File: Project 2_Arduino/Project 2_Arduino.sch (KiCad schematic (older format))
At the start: 16 parts, among them U2 LM1117-5.0, U3 ATMEGA328P-AU

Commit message: schematics USB UART added
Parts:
- added C4: 100nF, symbol C
- added U1: FT232RL, symbol FT232RL
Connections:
- wire segments 38 -> 48
- no-connect marks 0 -> 13
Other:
- moved on the sheet: C1, C3, C5, C7, R?, U3

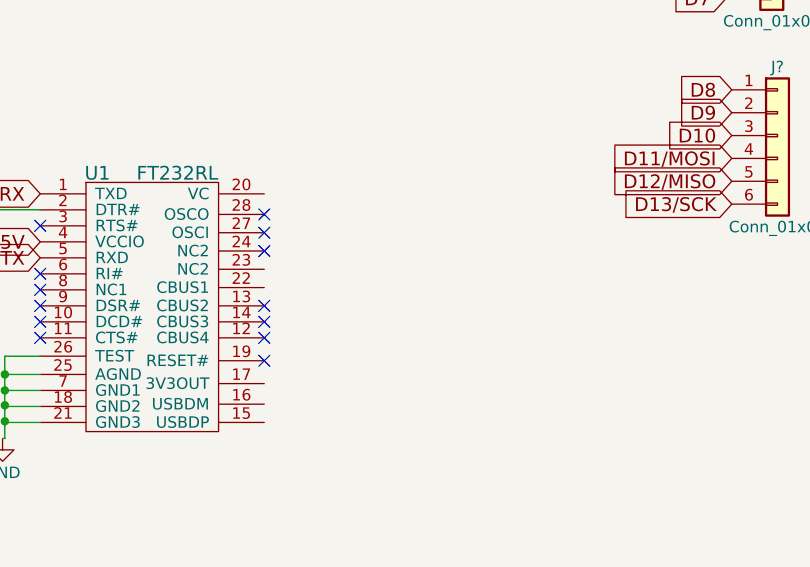
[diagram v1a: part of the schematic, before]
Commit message: USB to UART done
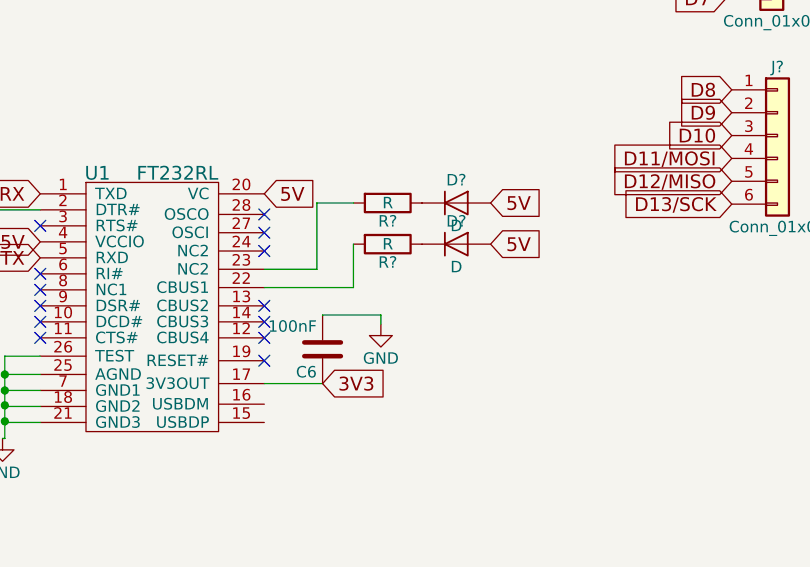
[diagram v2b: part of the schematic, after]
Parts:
- added C6: 100nF, symbol C
- added D? (x2): D, symbol D
- added R? (x2): R, symbol R
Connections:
- net labels added: 3V3
- wire segments 48 -> 56
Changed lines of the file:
@@
 Wire Wire Line
 	7095 4750 7085 4750
+Text GLabel 8230 3680 2    60   Input ~ 0
+5V
+$Comp
+L R R?
+U 1 1 59DF21B6
+P 8770 3900
+F 0 "R?" V 8850 3900 50  0000 C CNN
+F 1 "R" V 8770 3900 50  0000 C CNN
+F 2 "" V 8700 3900 50  0001 C CNN
+F 3 "" H 8770 3900 50  0001 C CNN
+	1    8770 3900
+	0    1    1    0
+$EndComp
+$Comp
+L D D?
+U 1 1 59DF2486
+P 9070 3720
+F 0 "D?" H 9070 3820 50  0000 C CNN
+F 1 "D" H 9070 3620 50  0000 C CNN
+F 2 "" H 9070 3720 50  0001 C CNN
+F 3 "" H 9070 3720 50  0001 C CNN
+	1    9070 3720
+	1    0    0    -1
+$EndComp
+$Comp
+L D D?
+U 1 1 59DF253A
+P 9070 3900
+F 0 "D?" H 9070 4000 50  0000 C CNN
+F 1 "D" H 9070 3800 50  0000 C CNN
+F 2 "" H 9070 3900 50  0001 C CNN
+F 3 "" H 9070 3900 50  0001 C CNN
+	1    9070 3900
+	1    0    0    -1
+$EndComp
+Text GLabel 9220 3720 2    60   Input ~ 0
+5V
+Text GLabel 9220 3900 2    60   Input ~ 0
+5V
+Wire Wire Line
+	8230 4090 8620 4090
+Wire Wire Line
+	8620 4090 8620 3900
+$Comp
+L R R?
+U 1 1 59DF2040
+P 8770 3720
+F 0 "R?" V 8850 3720 50  0000 C CNN
+F 1 "R" V 8770 3720 50  0000 C CNN
+F 2 "" V 8700 3720 50  0001 C CNN
+F 3 "" H 8770 3720 50  0001 C CNN
+	1    8770 3720
+	0    1    1    0
+$EndComp
+Wire Wire Line
+	8620 3720 8460 3720
+Wire Wire Line
+	8460 3720 8460 4010
+Wire Wire Line
+	8460 4010 8230 4010
+$Comp
+L C C6
+U 1 1 59DF2FE1
+P 8485 4360
+F 0 "C6" H 8510 4460 50  0000 L CNN
+F 1 "100nF" H 8510 4260 50  0000 L CNN
+F 2 "" H 8523 4210 50  0001 C CNN
+F 3 "" H 8485 4360 50  0001 C CNN
+	1    8485 4360
+	-1   0    0    1
+$EndComp
+Wire Wire Line
+	8230 4510 8485 4510
+Wire Wire Line
+	8485 4210 8740 4210
+Wire Wire Line
+	8740 4210 8740 4250
+$Comp
+L GND #PWR?
+U 1 1 59DF368B
+P 8740 4250
+F 0 "#PWR?" H 8740 4000 50  0001 C CNN
+F 1 "GND" H 8740 4100 50  0000 C CNN
+F 2 "" H 8740 4250 50  0001 C CNN
+F 3 "" H 8740 4250 50  0001 C CNN
+	1    8740 4250
+	1    0    0    -1
+$EndComp
+Text GLabel 8485 4510 2    60   Input ~ 0
+3V3
 $EndSCHEMATC

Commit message: first pass schematic done
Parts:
- removed C?: C, symbol C
- removed D?: D, symbol D
- removed R?: R, symbol R
- removed U2: LM1117-5.0, symbol LM1117-5.0
- added C2: 4.7uF_16V, symbol CP
- added C9: 100nF, symbol C
- added DL: D, symbol D
- added F1: Fuse, symbol Fuse
- added J3: USB_microB_2040002-1, symbol USB_microB_2040002-1
- added J4: Conn_02x03_Odd_Even, symbol Conn_02x03_Odd_Even
- added RD: 1K, symbol R
- added SW1: SW_Push, symbol SW_Push
- added Y1: 16MHz, symbol Crystal
- B, D, R2A, RA, RB: renamed from R?; value R -> 1K
- gave numbers to parts that had none: 3
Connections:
- net labels removed: VIN
- wire segments 56 -> 87
- no-connect marks 13 -> 14
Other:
- note added: "+5V Selector"
- note added: "Bypass Capacitors\n"
- note added: "Header Pins"
- note added: "ICSP\n"
- note added: "Microcontroller"
- note added: "Reset Switch"
- note added: "USB to UART"
- moved on the sheet: B, C1, C3, C4, C5, C6, C7, D, D1, DX1, DX2, J?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

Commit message: rearrange
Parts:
- gave numbers to parts that had none: 3
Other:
- moved on the sheet: B, C1, C2, C3, C4, C5, C6, C7, C9, D, D1, DL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

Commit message: caps edited
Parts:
- removed C2, C5: 4.7uF_16V, symbol CP
- added C2, C5: 10uF, symbol C
- added J13: Conn_01x03, symbol Conn_01x03
- renumbered DL to D3, RA to R1, RB to R2, B to R3, D to R4, R2A to R5, RD to R6
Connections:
- net D0 is gone; now on net D0/RX: J11.1 (Pin_1)
- net D1 is gone; now on net D1/TX: J11.2 (Pin_2)
- net 3V3: now also J13.2 (Pin_2)
- net 5V: now also C5.1, J13.1 (Pin_1)
- net GND: now also C2.2, C5.2, J13.3 (Pin_3)
- net VUSB: now also C2.1
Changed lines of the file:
@@
 $EndComp
 $Comp
-L GND #PWR?
+L GND #PWR01
 U 1 1 59DF0D4B
 P 1975 3875
-F 0 "#PWR?" H 1975 3625 50  0001 C CNN
+F 0 "#PWR01" H 1975 3625 50  0001 C CNN
 F 1 "GND" H 1975 3725 50  0000 C CNN
 F 2 "" H 1975 3875 50  0001 C CNN
@@
 A1
 Text GLabel 8700 5100 0    60   Input ~ 0
-D0
+D0/RX
 Text GLabel 8700 5200 0    60   Input ~ 0
-D1
+D1/TX
 Text GLabel 8700 5300 0    60   Input ~ 0
 D2
@@
 $EndComp
 $Comp
-L GND #PWR?
+L GND #PWR02
 U 1 1 59DEDBC3
 P 1825 2275
-F 0 "#PWR?" H 1825 2025 50  0001 C CNN
+F 0 "#PWR02" H 1825 2025 50  0001 C CNN
 F 1 "GND" H 1825 2125 50  0000 C CNN
 F 2 "" H 1825 2275 50  0001 C CNN
@@
 $EndComp
 $Comp
-L CP C5
-U 1 1 59DEDF72
-P 1100 1975
-F 0 "C5" H 1125 2075 50  0000 L CNN
-F 1 "4.7uF_16V" H 700 1875 50  0000 L CNN
-F 2 "" H 1138 1825 50  0001 C CNN
-F 3 "" H 1100 1975 50  0001 C CNN
-	1    1100 1975
-	1    0    0    -1
-$EndComp
-$Comp
-L GND #PWR?
+L GND #PWR03
 U 1 1 59DEE03F
 P 1375 2200
-F 0 "#PWR?" H 1375 1950 50  0001 C CNN
+F 0 "#PWR03" H 1375 1950 50  0001 C CNN
 F 1 "GND" H 1375 2050 50  0000 C CNN
 F 2 "" H 1375 2200 50  0001 C CNN
@@
 $EndComp
 $Comp
-L R R2A
+L R R5
 U 1 1 59DEEDB3
 P 4975 1600
-F 0 "R2A" V 5055 1600 50  0000 C CNN
+F 0 "R5" V 5055 1600 50  0000 C CNN
 F 1 "1K" V 4975 1600 50  0000 C CNN
 F 2 "" V 4905 1600 50  0001 C CNN
@@
 $EndComp
 $Comp
-L R RB
+L R R2
 U 1 1 59DEEEEE
 P 4950 3125
-F 0 "RB" V 5030 3125 50  0000 C CNN
+F 0 "R2" V 5030 3125 50  0000 C CNN
 F 1 "1K" V 4950 3125 50  0000 C CNN
 F 2 "" V 4880 3125 50  0001 C CNN
@@
 $EndComp
 $Comp
-L R RA
+L R R1
 U 1 1 59DEEF4E
 P 4950 3350
-F 0 "RA" V 5030 3350 50  0000 C CNN
+F 0 "R1" V 5030 3350 50  0000 C CNN
 F 1 "1K" V 4950 3350 50  0000 C CNN
 F 2 "" V 4880 3350 50  0001 C CNN
@@
 TX
 $Comp
-L GND #PWR?
+L GND #PWR04
 U 1 1 59DF0EF9
 P 7335 2650
-F 0 "#PWR?" H 7335 2400 50  0001 C CNN
+F 0 "#PWR04" H 7335 2400 50  0001 C CNN
 F 1 "GND" H 7335 2500 50  0000 C CNN
 F 2 "" H 7335 2650 50  0001 C CNN
@@
 5V
 $Comp
-L R D
+L R R4
 U 1 1 59DF21B6
 P 9020 1800
-F 0 "D" V 9100 1800 50  0000 C CNN
+F 0 "R4" V 9100 1800 50  0000 C CNN
 F 1 "1K" V 9020 1800 50  0000 C CNN
 F 2 "" V 8950 1800 50  0001 C CNN
@@
 5V
 $Comp
-L R B
+L R R3
 U 1 1 59DF2040
 P 9020 1620
-F 0 "B" V 9100 1620 50  0000 C CNN
+F 0 "R3" V 9100 1620 50  0000 C CNN
 F 1 "1K" V 9020 1620 50  0000 C CNN
 F 2 "" V 8950 1620 50  0001 C CNN
@@
 $EndComp
 $Comp
-L GND #PWR?
+L GND #PWR05
 U 1 1 59DF368B
 P 8990 2150
-F 0 "#PWR?" H 8990 1900 50  0001 C CNN
+F 0 "#PWR05" H 8990 1900 50  0001 C CNN
 F 1 "GND" H 8990 2000 50  0000 C CNN
 F 2 "" H 8990 2150 50  0001 C CNN
@@
 $EndComp
 $Comp
-L GND #PWR?
+L GND #PWR06
 U 1 1 59DF49F3
 P 10500 2475
-F 0 "#PWR?" H 10500 2225 50  0001 C CNN
+F 0 "#PWR06" H 10500 2225 50  0001 C CNN
 F 1 "GND" H 10500 2325 50  0000 C CNN
 F 2 "" H 10500 2475 50  0001 C CNN
@@
 D11/MOSI
 $Comp
-L GND #PWR?
+L GND #PWR07
 U 1 1 59DF7438
 P 5700 7125
-F 0 "#PWR?" H 5700 6875 50  0001 C CNN
+F 0 "#PWR07" H 5700 6875 50  0001 C CNN
 F 1 "GND" H 5700 6975 50  0000 C CNN
 F 2 "" H 5700 7125 50  0001 C CNN
@@
 $EndComp
 $Comp
-L GND #PWR?
+L GND #PWR08
 U 1 1 59DFC4DA
 P 1150 5925
-F 0 "#PWR?" H 1150 5675 50  0001 C CNN
+F 0 "#PWR08" H 1150 5675 50  0001 C CNN
 F 1 "GND" H 1150 5775 50  0000 C CNN
 F 2 "" H 1150 5925 50  0001 C CNN
@@
 RESET
 $Comp
-L R RD
+L R R6
 U 1 1 59DFCA3A
 P 1700 5675
-F 0 "RD" V 1780 5675 50  0000 C CNN
+F 0 "R6" V 1780 5675 50  0000 C CNN
 F 1 "1K" V 1700 5675 50  0000 C CNN
 F 2 "" V 1630 5675 50  0001 C CNN
@@
 Connection ~ 5275 2375
 $Comp
-L GND #PWR?
+L GND #PWR09
 U 1 1 59DFF36B
 P 5375 2425
-F 0 "#PWR?" H 5375 2175 50  0001 C CNN
+F 0 "#PWR09" H 5375 2175 50  0001 C CNN
 F 1 "GND" H 5375 2275 50  0000 C CNN
 F 2 "" H 5375 2425 50  0001 C CNN
@@
 Text Notes 7625 1275 0    197  ~ 0
 USB to UART
-$Comp
-L CP C2
-U 1 1 59E01805
-P 5075 5675
-F 0 "C2" H 5100 5775 50  0000 L CNN
-F 1 "4.7uF_16V" H 4675 5575 50  0000 L CNN
-F 2 "" H 5113 5525 50  0001 C CNN
-F 3 "" H 5075 5675 50  0001 C CNN
-	1    5075 5675
-	1    0    0    -1
-$EndComp
 $Comp
 L C C9
@@
 VUSB
 $Comp
-L GND #PWR?
+L GND #PWR010
 U 1 1 59E021A4
 P 5200 5950
-F 0 "#PWR?" H 5200 5700 50  0001 C CNN
+F 0 "#PWR010" H 5200 5700 50  0001 C CNN
 F 1 "GND" H 5200 5800 50  0000 C CNN
 F 2 "" H 5200 5950 50  0001 C CNN
@@
 Bypass Capacitors\n
 $Comp
-L D DL
+L D D3
 U 1 1 59E06E10
 P 5475 1600
-F 0 "DL" H 5475 1700 50  0000 C CNN
+F 0 "D3" H 5475 1700 50  0000 C CNN
 F 1 "D" H 5475 1500 50  0000 C CNN
 F 2 "" H 5475 1600 50  0001 C CNN
@@
 	5925 1600 5925 1650
 $Comp
-L GND #PWR?
+L GND #PWR011
 U 1 1 59E072C9
 P 5925 1650
-F 0 "#PWR?" H 5925 1400 50  0001 C CNN
+F 0 "#PWR011" H 5925 1400 50  0001 C CNN
 F 1 "GND" H 5925 1500 50  0000 C CNN
 F 2 "" H 5925 1650 50  0001 C CNN
@@
 	8825 3550 8700 3550
 $Comp
-L GND #PWR?
+L GND #PWR012
 U 1 1 59E0912F
 P 9225 2750
-F 0 "#PWR?" H 9225 2500 50  0001 C CNN
+F 0 "#PWR012" H 9225 2500 50  0001 C CNN
 F 1 "GND" H 9225 2600 50  0000 C CNN
 F 2 "" H 9225 2750 50  0001 C CNN
@@
 	1    0    0    -1
 $EndComp
+Text GLabel 10650 5375 0    60   Input ~ 0
+5V
+Text GLabel 10650 5475 0    60   Input ~ 0
+3V3
+Text GLabel 10650 5575 0    60   Input ~ 0
+GND
+$Comp
+L Conn_01x03 J13
+U 1 1 59E1247B
+P 10850 5475
+F 0 "J13" H 10850 5675 50  0000 C CNN
+F 1 "Conn_01x03" H 10850 5275 50  0000 C CNN
+F 2 "" H 10850 5475 50  0001 C CNN
+F 3 "" H 10850 5475 50  0001 C CNN
+	1    10850 5475
+	1    0    0    -1
+$EndComp
+$Comp
+L C C5
+U 1 1 59E133F2
+P 1100 1975
+F 0 "C5" H 1125 2075 50  0000 L CNN
+F 1 "10uF" H 1125 1875 50  0000 L CNN
+F 2 "" H 1138 1825 50  0001 C CNN
+F 3 "" H 1100 1975 50  0001 C CNN
+	1    1100 1975
+	1    0    0    -1
+$EndComp
+$Comp
+L C C2
+U 1 1 59E134E7
+P 5075 5675
+F 0 "C2" H 5100 5775 50  0000 L CNN
+F 1 "10uF" H 5100 5575 50  0000 L CNN
+F 2 "" H 5113 5525 50  0001 C CNN
+F 3 "" H 5075 5675 50  0001 C CNN
+	1    5075 5675
+	1    0    0    -1
+$EndComp
+$Comp
+L GND #PWR013
+U 1 1 59E142CF
+P 10300 4625
+F 0 "#PWR013" H 10300 4375 50  0001 C CNN
+F 1 "GND" H 10300 4475 50  0000 C CNN
+F 2 "" H 10300 4625 50  0001 C CNN
+F 3 "" H 10300 4625 50  0001 C CNN
+	1    10300 4625
+	1    0    0    -1
+$EndComp
+Wire Wire Line
+	10300 4625 10525 4625
+Text GLabel 10525 4625 2    60   Input ~ 0
+GND
 $EndSCHEMATC

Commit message: footprints associated
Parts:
- C1, C3, C4, C6, C7, C9: footprint (none) -> Capacitors_SMD:C_0603
- C2, C5: footprint (none) -> Capacitors_SMD:C_0805
- D1, D3, DX1, DX2: footprint (none) -> Diodes_SMD:D_0805
- F1: footprint (none) -> p2arduino:FuseSMD0603
- J10, J11: footprint (none) -> Pin_Headers:Pin_Header_Straight_1x08_Pitch1.00mm
- J12: footprint (none) -> Pin_Headers:Pin_Header_Straight_1x06_Pitch1.00mm
- J13: footprint (none) -> Pin_Headers:Pin_Header_Straight_1x03_Pitch1.00mm
- J3: footprint (none) -> Project 2_Arduino:USB_microB_2040002-1
- J4: footprint (none) -> Pin_Headers:Pin_Header_Straight_2x03_Pitch1.00mm
- R1, R2, R3, R4, R5, R6: footprint (none) -> Resistors_SMD:R_0603
- SW1: footprint (none) -> p2arduino:SPSTbtn
- U1: footprint (none) -> Housings_QFP:TQFP-32_7x7mm_Pitch0.8mm
- Y1: footprint (none) -> project2:TM16
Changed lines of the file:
@@
 F 0 "J10" H 8025 5775 50  0000 C CNN
 F 1 "Conn_01x08" H 8025 4875 50  0000 C CNN
-F 2 "" H 8025 5375 50  0001 C CNN
+F 2 "Pin_Headers:Pin_Header_Straight_1x08_Pitch1.00mm" H 8025 5375 50  0001 C CNN
 F 3 "" H 8025 5375 50  0001 C CNN
 	1    8025 5375
@@
 F 0 "J11" H 8900 5800 50  0000 C CNN
 F 1 "Conn_01x08" H 8900 4900 50  0000 C CNN
-F 2 "" H 8900 5400 50  0001 C CNN
+F 2 "Pin_Headers:Pin_Header_Straight_1x08_Pitch1.00mm" H 8900 5400 50  0001 C CNN
 F 3 "" H 8900 5400 50  0001 C CNN
 	1    8900 5400
@@
 F 0 "J12" H 10000 5750 50  0000 C CNN
 F 1 "Conn_01x06" H 10000 5050 50  0000 C CNN
-F 2 "" H 10000 5450 50  0001 C CNN
+F 2 "Pin_Headers:Pin_Header_Straight_1x06_Pitch1.00mm" H 10000 5450 50  0001 C CNN
 F 3 "" H 10000 5450 50  0001 C CNN
 	1    10000 5450
@@
 F 0 "C1" H 2075 2350 50  0000 L CNN
 F 1 "100nF" H 2075 2150 50  0000 L CNN
-F 2 "" H 2088 2100 50  0001 C CNN
+F 2 "Capacitors_SMD:C_0603" H 2088 2100 50  0001 C CNN
 F 3 "" H 2050 2250 50  0001 C CNN
 	1    2050 2250
@@
 F 0 "C3" H 1700 2075 50  0000 L CNN
 F 1 "1uF" H 1700 1875 50  0000 L CNN
-F 2 "" H 1713 1825 50  0001 C CNN
+F 2 "Capacitors_SMD:C_0603" H 1713 1825 50  0001 C CNN
 F 3 "" H 1675 1975 50  0001 C CNN
 	1    1675 1975
@@
 F 0 "C7" H 1400 2075 50  0000 L CNN
 F 1 "1uF" H 1400 1875 50  0000 L CNN
-F 2 "" H 1413 1825 50  0001 C CNN
+F 2 "Capacitors_SMD:C_0603" H 1413 1825 50  0001 C CNN
 F 3 "" H 1375 1975 50  0001 C CNN
 	1    1375 1975
@@
 F 0 "R5" V 5055 1600 50  0000 C CNN
 F 1 "1K" V 4975 1600 50  0000 C CNN
-F 2 "" V 4905 1600 50  0001 C CNN
+F 2 "Resistors_SMD:R_0603" V 4905 1600 50  0001 C CNN
 F 3 "" H 4975 1600 50  0001 C CNN
 	1    4975 1600
@@
 F 0 "R2" V 5030 3125 50  0000 C CNN
 F 1 "1K" V 4950 3125 50  0000 C CNN
-F 2 "" V 4880 3125 50  0001 C CNN
+F 2 "Resistors_SMD:R_0603" V 4880 3125 50  0001 C CNN
 F 3 "" H 4950 3125 50  0001 C CNN
 	1    4950 3125
@@
 F 0 "R1" V 5030 3350 50  0000 C CNN
 F 1 "1K" V 4950 3350 50  0000 C CNN
-F 2 "" V 4880 3350 50  0001 C CNN
+F 2 "Resistors_SMD:R_0603" V 4880 3350 50  0001 C CNN
 F 3 "" H 4950 3350 50  0001 C CNN
 	1    4950 3350
@@
 F 0 "D1" H 1800 7175 50  0000 C CNN
 F 1 "D" H 1800 6975 50  0000 C CNN
-F 2 "" H 1800 7075 50  0001 C CNN
+F 2 "Diodes_SMD:D_0805" H 1800 7075 50  0001 C CNN
 F 3 "" H 1800 7075 50  0001 C CNN
 	1    1800 7075
@@
 F 0 "U1" H 7750 2610 60  0000 C CNN
 F 1 "FT232RL" H 8100 2610 60  0000 C CNN
-F 2 "" H 7970 2050 60  0001 C CNN
+F 2 "Housings_QFP:TQFP-32_7x7mm_Pitch0.8mm" H 7970 2050 60  0001 C CNN
 F 3 "" H 7970 2050 60  0001 C CNN
 	1    8000 2050
@@
 F 0 "C4" H 7150 1750 50  0000 L CNN
 F 1 "100nF" H 7150 1550 50  0000 L CNN
-F 2 "" H 7163 1500 50  0001 C CNN
+F 2 "Capacitors_SMD:C_0603" H 7163 1500 50  0001 C CNN
 F 3 "" H 7125 1650 50  0001 C CNN
 	1    7125 1650
@@
 F 0 "R4" V 9100 1800 50  0000 C CNN
 F 1 "1K" V 9020 1800 50  0000 C CNN
-F 2 "" V 8950 1800 50  0001 C CNN
+F 2 "Resistors_SMD:R_0603" V 8950 1800 50  0001 C CNN
 F 3 "" H 9020 1800 50  0001 C CNN
 	1    9020 1800
@@
 F 0 "DX1" H 9320 1720 50  0000 C CNN
 F 1 "D" H 9320 1520 50  0000 C CNN
-F 2 "" H 9320 1620 50  0001 C CNN
+F 2 "Diodes_SMD:D_0805" H 9320 1620 50  0001 C CNN
 F 3 "" H 9320 1620 50  0001 C CNN
 	1    9320 1620
@@
 F 0 "DX2" H 9320 1900 50  0000 C CNN
 F 1 "D" H 9320 1700 50  0000 C CNN
-F 2 "" H 9320 1800 50  0001 C CNN
+F 2 "Diodes_SMD:D_0805" H 9320 1800 50  0001 C CNN
 F 3 "" H 9320 1800 50  0001 C CNN
 	1    9320 1800
@@
 F 0 "R3" V 9100 1620 50  0000 C CNN
 F 1 "1K" V 9020 1620 50  0000 C CNN
-F 2 "" V 8950 1620 50  0001 C CNN
+F 2 "Resistors_SMD:R_0603" V 8950 1620 50  0001 C CNN
 F 3 "" H 9020 1620 50  0001 C CNN
 	1    9020 1620
@@
 F 0 "C6" H 8760 2360 50  0000 L CNN
 F 1 "100nF" H 8760 2160 50  0000 L CNN
-F 2 "" H 8773 2110 50  0001 C CNN
+F 2 "Capacitors_SMD:C_0603" H 8773 2110 50  0001 C CNN
 F 3 "" H 8735 2260 50  0001 C CNN
 	1    8735 2260
@@
 F 0 "J3" H 9425 3800 60  0000 L CNN
 F 1 "USB_microB_2040002-1" H 9425 3700 60  0000 L CNN
-F 2 "" H 10225 3300 50  0001 C CNN
+F 2 "Project 2_Arduino:USB_microB_2040002-1" H 10225 3300 50  0001 C CNN
 F 3 "" H 10225 3300 50  0001 C CNN
 	1    9875 3150
@@
 F 0 "F1" V 9055 3550 50  0000 C CNN
 F 1 "Fuse" V 8900 3550 50  0000 C CNN
-F 2 "" V 8905 3550 50  0001 C CNN
+F 2 "p2arduino:FuseSMD0603" V 8905 3550 50  0001 C CNN
 F 3 "" H 8975 3550 50  0001 C CNN
 	1    8975 3550
@@
 F 0 "J4" H 5450 7225 50  0000 C CNN
 F 1 "Conn_02x03_Odd_Even" H 5475 7300 50  0000 C CNN
-F 2 "" H 5400 7025 50  0001 C CNN
+F 2 "Pin_Headers:Pin_Header_Straight_2x03_Pitch1.00mm" H 5400 7025 50  0001 C CNN
 F 3 "" H 5400 7025 50  0001 C CNN
 	1    5400 7025
@@
 F 0 "SW1" H 1450 6025 50  0000 L CNN
 F 1 "SW_Push" H 1400 5865 50  0000 C CNN
-F 2 "" H 1400 6125 50  0001 C CNN
+F 2 "p2arduino:SPSTbtn" H 1400 6125 50  0001 C CNN
 F 3 "" H 1400 6125 50  0001 C CNN
 	1    1400 5925
@@
 F 0 "R6" V 1780 5675 50  0000 C CNN
 F 1 "1K" V 1700 5675 50  0000 C CNN
-F 2 "" V 1630 5675 50  0001 C CNN
+F 2 "Resistors_SMD:R_0603" V 1630 5675 50  0001 C CNN
 F 3 "" H 1700 5675 50  0001 C CNN
 	1    1700 5675
@@
 F 0 "Y1" H 5075 2550 50  0000 C CNN
 F 1 "16MHz" H 5075 2250 50  0000 C CNN
-F 2 "" H 5075 2400 50  0001 C CNN
+F 2 "project2:TM16" H 5075 2400 50  0001 C CNN
 F 3 "" H 5075 2400 50  0001 C CNN
 	1    5075 2400
@@
 F 0 "C9" H 5375 5775 50  0000 L CNN
 F 1 "100nF" H 5375 5575 50  0000 L CNN
-F 2 "" H 5388 5525 50  0001 C CNN
+F 2 "Capacitors_SMD:C_0603" H 5388 5525 50  0001 C CNN
 F 3 "" H 5350 5675 50  0001 C CNN
 	1    5350 5675
@@
 F 0 "D3" H 5475 1700 50  0000 C CNN
 F 1 "D" H 5475 1500 50  0000 C CNN
-F 2 "" H 5475 1600 50  0001 C CNN
+F 2 "Diodes_SMD:D_0805" H 5475 1600 50  0001 C CNN
 F 3 "" H 5475 1600 50  0001 C CNN
 	1    5475 1600
@@
 F 0 "J13" H 10850 5675 50  0000 C CNN
 F 1 "Conn_01x03" H 10850 5275 50  0000 C CNN
-F 2 "" H 10850 5475 50  0001 C CNN
+F 2 "Pin_Headers:Pin_Header_Straight_1x03_Pitch1.00mm" H 10850 5475 50  0001 C CNN
 F 3 "" H 10850 5475 50  0001 C CNN
 	1    10850 5475
@@
 F 0 "C5" H 1125 2075 50  0000 L CNN
 F 1 "10uF" H 1125 1875 50  0000 L CNN
-F 2 "" H 1138 1825 50  0001 C CNN
+F 2 "Capacitors_SMD:C_0805" H 1138 1825 50  0001 C CNN
 F 3 "" H 1100 1975 50  0001 C CNN
 	1    1100 1975
@@
 F 0 "C2" H 5100 5775 50  0000 L CNN
 F 1 "10uF" H 5100 5575 50  0000 L CNN
-F 2 "" H 5113 5525 50  0001 C CNN
+F 2 "Capacitors_SMD:C_0805" H 5113 5525 50  0001 C CNN
 F 3 "" H 5075 5675 50  0001 C CNN
 	1    5075 5675

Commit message: new crystal
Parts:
- added Y?: Crystal_GND24, symbol Crystal_GND24
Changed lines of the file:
@@
 Text GLabel 10525 4625 2    60   Input ~ 0
 GND
+$Comp
+L Crystal_GND24 Y?
+U 1 1 59DF0F95
+P 5725 2375
+F 0 "Y?" H 5850 2575 50  0000 L CNN
+F 1 "Crystal_GND24" H 5850 2500 50  0000 L CNN
+F 2 "" H 5725 2375 50  0001 C CNN
+F 3 "" H 5725 2375 50  0001 C CNN
+	1    5725 2375
+	1    0    0    -1
+$EndComp
 $EndSCHEMATC
